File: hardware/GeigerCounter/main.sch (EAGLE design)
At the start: 34 parts, among them IC1 LM358N, T2 BC848ALT1SMD, T3 IRF840, T4 , T5 BD139, T6 BC848ALT1SMD, T7 BC848ALT1SMD

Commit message: Fixed PCB.
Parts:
- removed C3: (no value), resistor:C-EU102-054X133
- T5: value BD139 -> BC848ALT1SMD; device transistor:BD139 -> transistor-npn:BC848ALT1SMD
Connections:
- net N$12: no longer C3.1
- net N$5: no longer C3.2
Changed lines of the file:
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@@
 <part name="R13" library="resistor" deviceset="R-EU_" device="M1206"/>
 <part name="R11" library="resistor" deviceset="R-EU_" device="M1206"/>
-<part name="T5" library="transistor" deviceset="BD139" device="" value=""/>
 <part name="C5" library="resistor" deviceset="CPOL-EU" device="E5-8.5"/>
 <part name="LED1" library="led" deviceset="LED" device="SFH482"/>
@@
 <part name="L1" library="resistor" deviceset="L-EU" device="TJ5-U1"/>
 <part name="C2" library="resistor" deviceset="C-EU" device="102-054X133"/>
-<part name="C3" library="resistor" deviceset="C-EU" device="102-054X133"/>
+<part name="T5" library="transistor-npn" deviceset="BC848*" device="SMD" technology="ALT1" value=""/>
 </parts>
 <sheets>
@@
 <attribute name="VALUE" x="13.97" y="47.498" size="1.778" layer="96"/>
 </instance>
-<instance part="T5" gate="G$1" x="27.94" y="50.8" smashed="yes">
-<attribute name="NAME" x="25.4" y="45.72" size="1.778" layer="95"/>
-<attribute name="VALUE" x="17.78" y="55.88" size="1.778" layer="96"/>
-</instance>
 <instance part="C5" gate="G$1" x="86.36" y="53.34"/>
 <instance part="LED1" gate="G$1" x="43.18" y="58.42"/>
@@
 <instance part="L1" gate="G$1" x="-71.12" y="66.04"/>
 <instance part="C2" gate="G$1" x="-40.64" y="45.72"/>
-<instance part="C3" gate="G$1" x="-33.02" y="45.72"/>
+<instance part="T5" gate="G$1" x="27.94" y="50.8" smashed="yes">
+<attribute name="NAME" x="25.4" y="45.72" size="1.778" layer="95"/>
+<attribute name="VALUE" x="17.78" y="55.88" size="1.778" layer="96"/>
+</instance>
 </instances>
 <busses>
@@
 <wire x1="91.44" y1="25.4" x2="86.36" y2="25.4" width="0.1524" layer="91"/>
 <junction x="43.18" y="25.4"/>
-<pinref part="T5" gate="G$1" pin="E"/>
 <wire x1="86.36" y1="25.4" x2="81.28" y2="25.4" width="0.1524" layer="91"/>
 <wire x1="81.28" y1="25.4" x2="58.42" y2="25.4" width="0.1524" layer="91"/>
 <wire x1="58.42" y1="25.4" x2="55.88" y2="25.4" width="0.1524" layer="91"/>
 <wire x1="55.88" y1="25.4" x2="50.8" y2="25.4" width="0.1524" layer="91"/>
-<wire x1="30.48" y1="45.72" x2="30.48" y2="25.4" width="0.1524" layer="91"/>
-<junction x="30.48" y="25.4"/>
 <junction x="81.28" y="25.4"/>
 <pinref part="R3" gate="G$1" pin="1"/>
@@
 <wire x1="30.48" y1="25.4" x2="-10.16" y2="25.4" width="0.1524" layer="91"/>
 <wire x1="-10.16" y1="25.4" x2="-15.24" y2="25.4" width="0.1524" layer="91"/>
-<wire x1="-15.24" y1="25.4" x2="-33.02" y2="25.4" width="0.1524" layer="91"/>
-<wire x1="-33.02" y1="25.4" x2="-40.64" y2="25.4" width="0.1524" layer="91"/>
+<wire x1="-15.24" y1="25.4" x2="-40.64" y2="25.4" width="0.1524" layer="91"/>
 <wire x1="-40.64" y1="25.4" x2="-45.72" y2="25.4" width="0.1524" layer="91"/>
 <wire x1="-45.72" y1="25.4" x2="-45.72" y2="30.48" width="0.1524" layer="91"/>
@@
 <wire x1="-40.64" y1="40.64" x2="-40.64" y2="25.4" width="0.1524" layer="91"/>
 <junction x="-40.64" y="25.4"/>
-<pinref part="C3" gate="G$1" pin="2"/>
-<wire x1="-33.02" y1="40.64" x2="-33.02" y2="25.4" width="0.1524" layer="91"/>
-<junction x="-33.02" y="25.4"/>
 <pinref part="SV4(POWER)" gate="G$1" pin="1"/>
 <wire x1="93.98" y1="50.8" x2="91.44" y2="50.8" width="0.1524" layer="91"/>
@@
 <wire x1="86.36" y1="48.26" x2="86.36" y2="25.4" width="0.1524" layer="91"/>
 <junction x="86.36" y="25.4"/>
+<pinref part="T5" gate="G$1" pin="E"/>
+<wire x1="30.48" y1="45.72" x2="30.48" y2="25.4" width="0.1524" layer="91"/>
+<junction x="30.48" y="25.4"/>
 </segment>
 </net>
@@
 </segment>
 </net>
-<net name="N$9" class="0">
-<segment>
-<pinref part="R11" gate="G$1" pin="2"/>
-<pinref part="T5" gate="G$1" pin="B"/>
-<wire x1="22.86" y1="50.8" x2="25.4" y2="50.8" width="0.1524" layer="91"/>
-</segment>
-</net>
 <net name="N$6" class="0">
 <segment>
@@
 <pinref part="R5" gate="G$1" pin="1"/>
 <pinref part="C2" gate="G$1" pin="1"/>
-<wire x1="-40.64" y1="68.58" x2="-33.02" y2="68.58" width="0.1524" layer="91"/>
-<wire x1="-33.02" y1="68.58" x2="-30.48" y2="68.58" width="0.1524" layer="91"/>
+<wire x1="-40.64" y1="68.58" x2="-30.48" y2="68.58" width="0.1524" layer="91"/>
 <wire x1="-40.64" y1="48.26" x2="-40.64" y2="68.58" width="0.1524" layer="91"/>
 <junction x="-40.64" y="68.58"/>
-<pinref part="C3" gate="G$1" pin="1"/>
-<wire x1="-33.02" y1="48.26" x2="-33.02" y2="68.58" width="0.1524" layer="91"/>
-<junction x="-33.02" y="68.58"/>
-</segment>
-</net>
-<net name="N$13" class="0">
-<segment>
-<pinref part="SP1" gate="G$1" pin="2"/>
-<pinref part="T5" gate="G$1" pin="C"/>
-<wire x1="30.48" y1="58.42" x2="30.48" y2="55.88" width="0.1524" layer="91"/>
 </segment>
 </net>
@@
 </segment>
 </net>
+<net name="N$9" class="0">
+<segment>
+<pinref part="R11" gate="G$1" pin="2"/>
+<pinref part="T5" gate="G$1" pin="B"/>
+<wire x1="22.86" y1="50.8" x2="25.4" y2="50.8" width="0.1524" layer="91"/>
+</segment>
+</net>
+<net name="N$13" class="0">
+<segment>
+<pinref part="SP1" gate="G$1" pin="2"/>
+<pinref part="T5" gate="G$1" pin="C"/>
+<wire x1="30.48" y1="58.42" x2="30.48" y2="55.88" width="0.1524" layer="91"/>
+</segment>
+</net>

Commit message: Built and tested version.
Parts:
- removed SV1(PWM): (no value), con-lstb:MA04-1
- removed T4: (no value), transistor-npn:BC848ALT1SMD
- removed T5: BC848ALT1SMD, transistor-npn:BC848ALT1SMD
- added C3: (no value), resistor:C-EU050-025X075
- added C6, C7: 330u, resistor:CPOL-USA/3216-18W
- added D2: BAS40, diode:BAS40
- added IC2: (no value), ic-package:DIL8
- C1: device resistor:C-EU050-050X075 -> resistor:C-EU050-025X075
- C2: device resistor:C-EU102-054X133 -> resistor:C-EUC3216
- C4: device resistor:C-EUC3216 -> resistor:C-EU102-064X133
- C5: value (none) -> 100n; device resistor:CPOL-EUE5-8.5 -> resistor:C-EUC3216
- IC1: value LM358N -> LM358D; device linear:LM358N -> linear:LM358D
- L1: device resistor:L-EUTJ5-U1 -> resistor:L-EU0207/5V
- R1: device resistor:R-EU_M1206 -> resistor:R-EU_0207/5V
- R10, R11, R9: value (none) -> 1k
- R12: value (none) -> 510R
- SP1: value AL60P -> 8R; device buzzer:AL60P -> buzzer:KSS1201
- T3: device transistor-fet:IRF840 -> transistor-power:BUZ11BV
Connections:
- removed net N$14: R1.1, SV1(PWM).3
- removed net N$7: C4.1, C5.+, IC1P.V+, L1.1, R12.2, R2.2, R8.2, SP1.1, SV1(PWM).4, SV4(POWER).3, T2.C
- new net V+: C2.1, C5.1, C6.+, C7.+, IC1P.V+, IC2.6, L1.1, R1.2, R12.2, R8.2, SP1.1, SV4(POWER).3
- new net V-: C1.2, C2.2, C3.2, C4.2, C5.2, C6.-, C7.-, IC1B.+IN, IC1P.V-, IC2.4, R2.1, R3.1, R6.1, R7.1, SV3(OUT).1, SV4(POWER).1, T1.C, T2.E, T3.S, T6.E, T7.E
- net N$10: now also R11.2, T2.B; no longer C1.1, R3.2, R4.1, T4.B
- net N$11: now also IC2.1, IC2.7, IC2.8, R1.1; no longer R2.1, SV1(PWM).2, T4.C
- net N$12: now also C4.1; no longer C2.1
- net N$13: now also C3.1, IC2.5, R3.2, R4.1; no longer SP1.2, T5.C
- net N$16: now also D2.C; no longer T2.E
- net N$18: now also D2.A, IC2.3, R2.2; no longer R1.2, T2.B
- net N$5: now also C1.1, IC2.2; no longer C1.2, C2.2, C4.2, C5.-, IC1B.+IN, IC1P.V-, R3.1, R6.1, R7.1, SV1(PWM).1, SV3(OUT).1, SV4(POWER).1, T1.C, T3.S, T4.E, T5.E, T6.E, T7.E
- net N$9: now also SP1.2, T2.C; no longer R11.2, T5.B
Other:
- moved on the sheet: C1, C2, C4, D1, L1, R1, R2, R3, R4, SV4(POWER), T1, T2

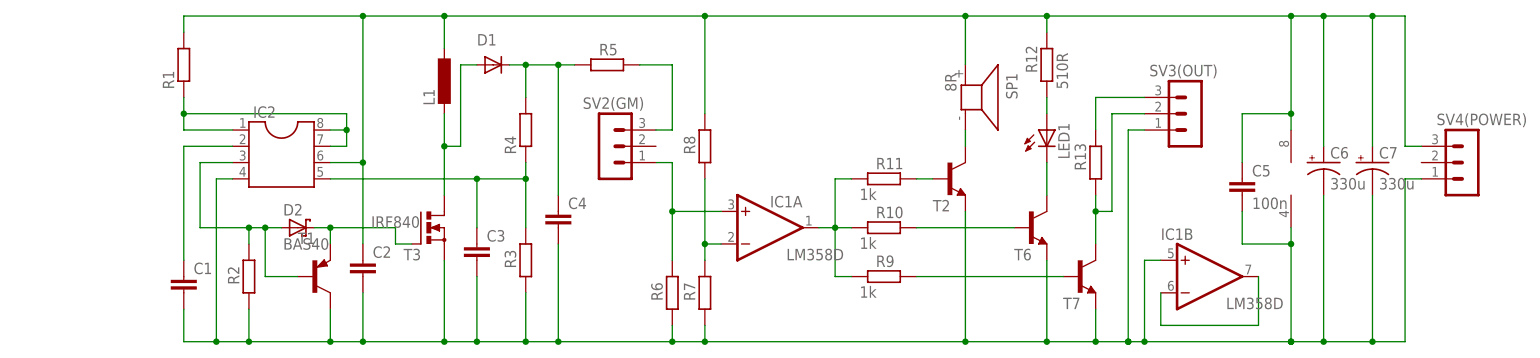
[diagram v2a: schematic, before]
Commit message: Fixed as is on HW model.
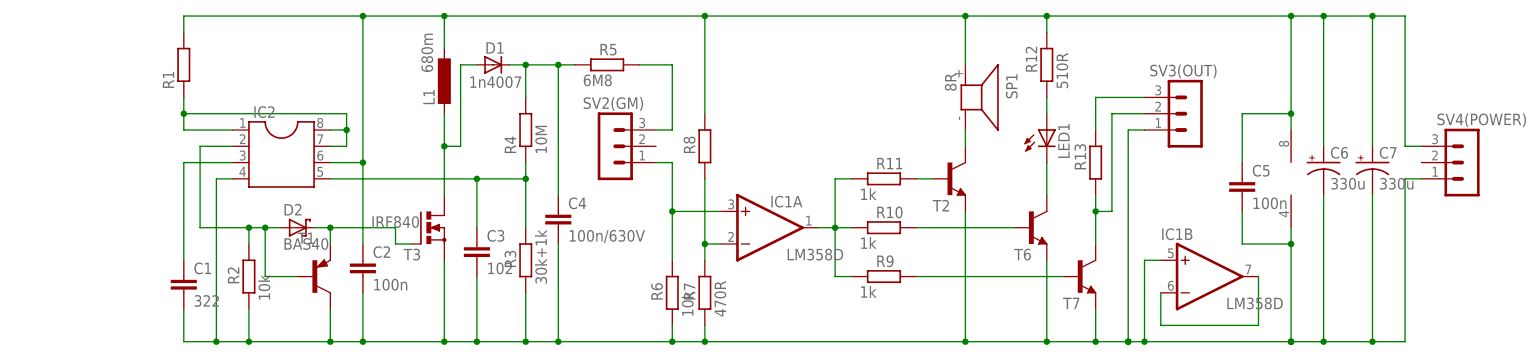
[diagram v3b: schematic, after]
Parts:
- C1: value (none) -> 322
- C2: value (none) -> 100n
- C3: value (none) -> 102
- C4: value (none) -> 100n/630V
- D1: value 1N4004 -> 1n4007
- L1: value (none) -> 680m
- R2, R6: value (none) -> 10k
- R3: value (none) -> 30k+1k
- R4: value (none) -> 10M
- R5: value (none) -> 6M8
- R7: value (none) -> 470R
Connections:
- removed net N$18: D2.A, IC2.3, R2.2, T1.B
- new net N$14: D2.A, IC2.2, R2.2, T1.B
- net N$5: now also IC2.3; no longer IC2.2
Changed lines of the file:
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@@
 <setting verticaltext="up"/>
 </settings>
-<grid distance="0.1" unitdist="inch" unit="inch" style="lines" multiple="1" display="no" altdistance="0.01" altunitdist="inch" altunit="inch"/>
+<grid distance="0.05" unitdist="inch" unit="inch" style="lines" multiple="1" display="yes" altdistance="0.01" altunitdist="inch" altunit="inch"/>
 <layers>
 <layer number="1" name="Top" color="4" fill="1" visible="no" active="no"/>
@@
 <part name="C6" library="resistor" deviceset="CPOL-US" device="A/3216-18W" value="330u"/>
 <part name="LED1" library="led" deviceset="LED" device="SFH482"/>
-<part name="R4" library="resistor" deviceset="R-EU_" device="0207/5V"/>
-<part name="R3" library="resistor" deviceset="R-EU_" device="0207/5V"/>
-<part name="D1" library="diode" deviceset="1N4004" device="" value=""/>
-<part name="R6" library="resistor" deviceset="R-EU_" device="0207/5V"/>
+<part name="R4" library="resistor" deviceset="R-EU_" device="0207/5V" value="10M"/>
+<part name="R3" library="resistor" deviceset="R-EU_" device="0207/5V" value="30k+1k"/>
+<part name="D1" library="diode" deviceset="1N4004" device="" value="1n4007"/>
+<part name="R6" library="resistor" deviceset="R-EU_" device="0207/5V" value="10k"/>
 <part name="SP1" library="buzzer" deviceset="KSS1201" device="" value="8R"/>
 <part name="T3" library="transistor-power" deviceset="BUZ11" device="BV" value="IRF840"/>
 <part name="T1" library="transistor" deviceset="*-PNP-" device="SOT23-BEC" technology="BC807-40"/>
 <part name="IC1" library="linear" deviceset="LM358" device="D" value="LM358D"/>
-<part name="R7" library="resistor" deviceset="R-EU_" device="0207/5V"/>
+<part name="R7" library="resistor" deviceset="R-EU_" device="0207/5V" value="470R"/>
 <part name="R8" library="resistor" deviceset="R-EU_" device="0207/5V"/>
 <part name="SV3(OUT)" library="con-lstb" deviceset="MA03-1" device=""/>
 <part name="SV2(GM)" library="con-lstb" deviceset="MA03-1" device=""/>
 <part name="SV4(POWER)" library="con-lstb" deviceset="MA03-1" device=""/>
-<part name="C3" library="resistor" deviceset="C-EU" device="050-025X075"/>
-<part name="R5" library="resistor" deviceset="R-EU_" device="0207/12"/>
+<part name="C3" library="resistor" deviceset="C-EU" device="050-025X075" value="102"/>
+<part name="R5" library="resistor" deviceset="R-EU_" device="0207/12" value="6M8"/>
 <part name="C5" library="resistor" deviceset="C-EU" device="C3216" value="100n"/>
-<part name="L1" library="resistor" deviceset="L-EU" device="0207/5V"/>
-<part name="C4" library="resistor" deviceset="C-EU" device="102-064X133"/>
-<part name="R2" library="resistor" deviceset="R-EU_" device="0207/5V"/>
+<part name="L1" library="resistor" deviceset="L-EU" device="0207/5V" value="680m"/>
+<part name="C4" library="resistor" deviceset="C-EU" device="102-064X133" value="100n/630V"/>
+<part name="R2" library="resistor" deviceset="R-EU_" device="0207/5V" value="10k"/>
 <part name="D2" library="diode" deviceset="BAS40" device=""/>
 <part name="T2" library="transistor-npn" deviceset="BC848*" device="SMD" technology="ALT1" value=""/>
 <part name="IC2" library="ic-package" deviceset="DIL8" device=""/>
-<part name="C1" library="resistor" deviceset="C-EU" device="050-025X075"/>
+<part name="C1" library="resistor" deviceset="C-EU" device="050-025X075" value="322"/>
 <part name="R1" library="resistor" deviceset="R-EU_" device="0207/5V"/>
-<part name="C2" library="resistor" deviceset="C-EU" device="C3216"/>
+<part name="C2" library="resistor" deviceset="C-EU" device="C3216" value="100n"/>
 <part name="C7" library="resistor" deviceset="CPOL-US" device="A/3216-18W" value="330u"/>
 </parts>
@@
 </instance>
 <instance part="D1" gate="1" x="-43.18" y="68.58" smashed="yes">
-<attribute name="NAME" x="-45.72" y="71.6026" size="1.778" layer="95"/>
-<attribute name="VALUE" x="-40.64" y="66.2686" size="1.778" layer="96"/>
+<attribute name="NAME" x="-44.45" y="70.3326" size="1.778" layer="95"/>
+<attribute name="VALUE" x="-46.99" y="64.9986" size="1.778" layer="96"/>
 </instance>
 <instance part="R6" gate="G$1" x="-15.24" y="33.02" smashed="yes" rot="R90">
@@
 </instance>
 <instance part="C5" gate="G$1" x="73.66" y="50.8"/>
-<instance part="L1" gate="G$1" x="-50.8" y="66.04"/>
+<instance part="L1" gate="G$1" x="-50.8" y="66.04" smashed="yes">
+<attribute name="NAME" x="-52.2986" y="62.23" size="1.778" layer="95" rot="R90"/>
+<attribute name="VALUE" x="-52.578" y="67.31" size="1.778" layer="96" rot="R90"/>
+</instance>
 <instance part="C4" gate="G$1" x="-33.02" y="45.72"/>
 <instance part="R2" gate="G$1" x="-81.28" y="35.56" smashed="yes" rot="R90">
@@
 <wire x1="-68.58" y1="43.18" x2="-71.12" y2="43.18" width="0.1524" layer="91"/>
 <junction x="-68.58" y="43.18"/>
-</segment>
-</net>
-<net name="N$18" class="0">
-<segment>
-<pinref part="T1" gate="G$1" pin="B"/>
-<wire x1="-78.74" y1="43.18" x2="-78.74" y2="35.56" width="0.1524" layer="91"/>
-<wire x1="-78.74" y1="35.56" x2="-73.66" y2="35.56" width="0.1524" layer="91"/>
-<pinref part="R2" gate="G$1" pin="2"/>
-<wire x1="-81.28" y1="40.64" x2="-81.28" y2="43.18" width="0.1524" layer="91"/>
-<wire x1="-81.28" y1="43.18" x2="-78.74" y2="43.18" width="0.1524" layer="91"/>
-<pinref part="D2" gate="1" pin="A"/>
-<wire x1="-78.74" y1="43.18" x2="-76.2" y2="43.18" width="0.1524" layer="91"/>
-<junction x="-78.74" y="43.18"/>
-<wire x1="-81.28" y1="43.18" x2="-88.9" y2="43.18" width="0.1524" layer="91"/>
-<wire x1="-88.9" y1="43.18" x2="-88.9" y2="53.34" width="0.1524" layer="91"/>
-<junction x="-81.28" y="43.18"/>
-<pinref part="IC2" gate="G$1" pin="3"/>
-<wire x1="-88.9" y1="53.34" x2="-83.82" y2="53.34" width="0.1524" layer="91"/>
 </segment>
 </net>
@@
 <segment>
 <pinref part="C1" gate="G$1" pin="1"/>
-<wire x1="-91.44" y1="38.1" x2="-91.44" y2="55.88" width="0.1524" layer="91"/>
+<wire x1="-91.44" y1="38.1" x2="-91.44" y2="53.34" width="0.1524" layer="91"/>
+<pinref part="IC2" gate="G$1" pin="3"/>
+<wire x1="-83.82" y1="53.34" x2="-91.44" y2="53.34" width="0.1524" layer="91"/>
+</segment>
+</net>
+<net name="N$14" class="0">
+<segment>
 <pinref part="IC2" gate="G$1" pin="2"/>
-<wire x1="-91.44" y1="55.88" x2="-83.82" y2="55.88" width="0.1524" layer="91"/>
-</segment>
-</net>
+<wire x1="-83.82" y1="55.88" x2="-88.9" y2="55.88" width="0.1524" layer="91"/>
+<pinref part="T1" gate="G$1" pin="B"/>
+<wire x1="-78.74" y1="43.18" x2="-78.74" y2="35.56" width="0.1524" layer="91"/>
+<wire x1="-78.74" y1="35.56" x2="-73.66" y2="35.56" width="0.1524" layer="91"/>
+<pinref part="R2" gate="G$1" pin="2"/>
+<wire x1="-81.28" y1="40.64" x2="-81.28" y2="43.18" width="0.1524" layer="91"/>
+<wire x1="-81.28" y1="43.18" x2="-78.74" y2="43.18" width="0.1524" layer="91"/>
+<pinref part="D2" gate="1" pin="A"/>
+<wire x1="-78.74" y1="43.18" x2="-76.2" y2="43.18" width="0.1524" layer="91"/>
+<junction x="-78.74" y="43.18"/>
+<wire x1="-81.28" y1="43.18" x2="-88.9" y2="43.18" width="0.1524" layer="91"/>
+<wire x1="-88.9" y1="43.18" x2="-88.9" y2="55.88" width="0.1524" layer="91"/>
+<junction x="-81.28" y="43.18"/>
+</segment>
+</net>
